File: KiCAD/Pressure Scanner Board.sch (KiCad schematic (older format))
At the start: 23 parts

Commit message: Pinned pressure sensors and added 3.3V - 5V level shifter
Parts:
- removed J? (x2): .1\" Headers, Pin_Headers:Pin_Header_Straight_1x20_Pitch2.54mm, symbol Conn_01x20
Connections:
- net labels removed: +5V, PA10, PA11, PA12, PA13, PA14, PA15, PA16, PA17, PA18, PA19, PA2, PA20, PA21, PA22, PA23, PA28, PA3, PA4, PA5, PA6, PA7, PA8, PA9, PB10, PB11, PB2, PB22, PB23, PB8, PB9, VIN
- wire segments 151 -> 78
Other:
- note removed: "0.100" Headers\n"

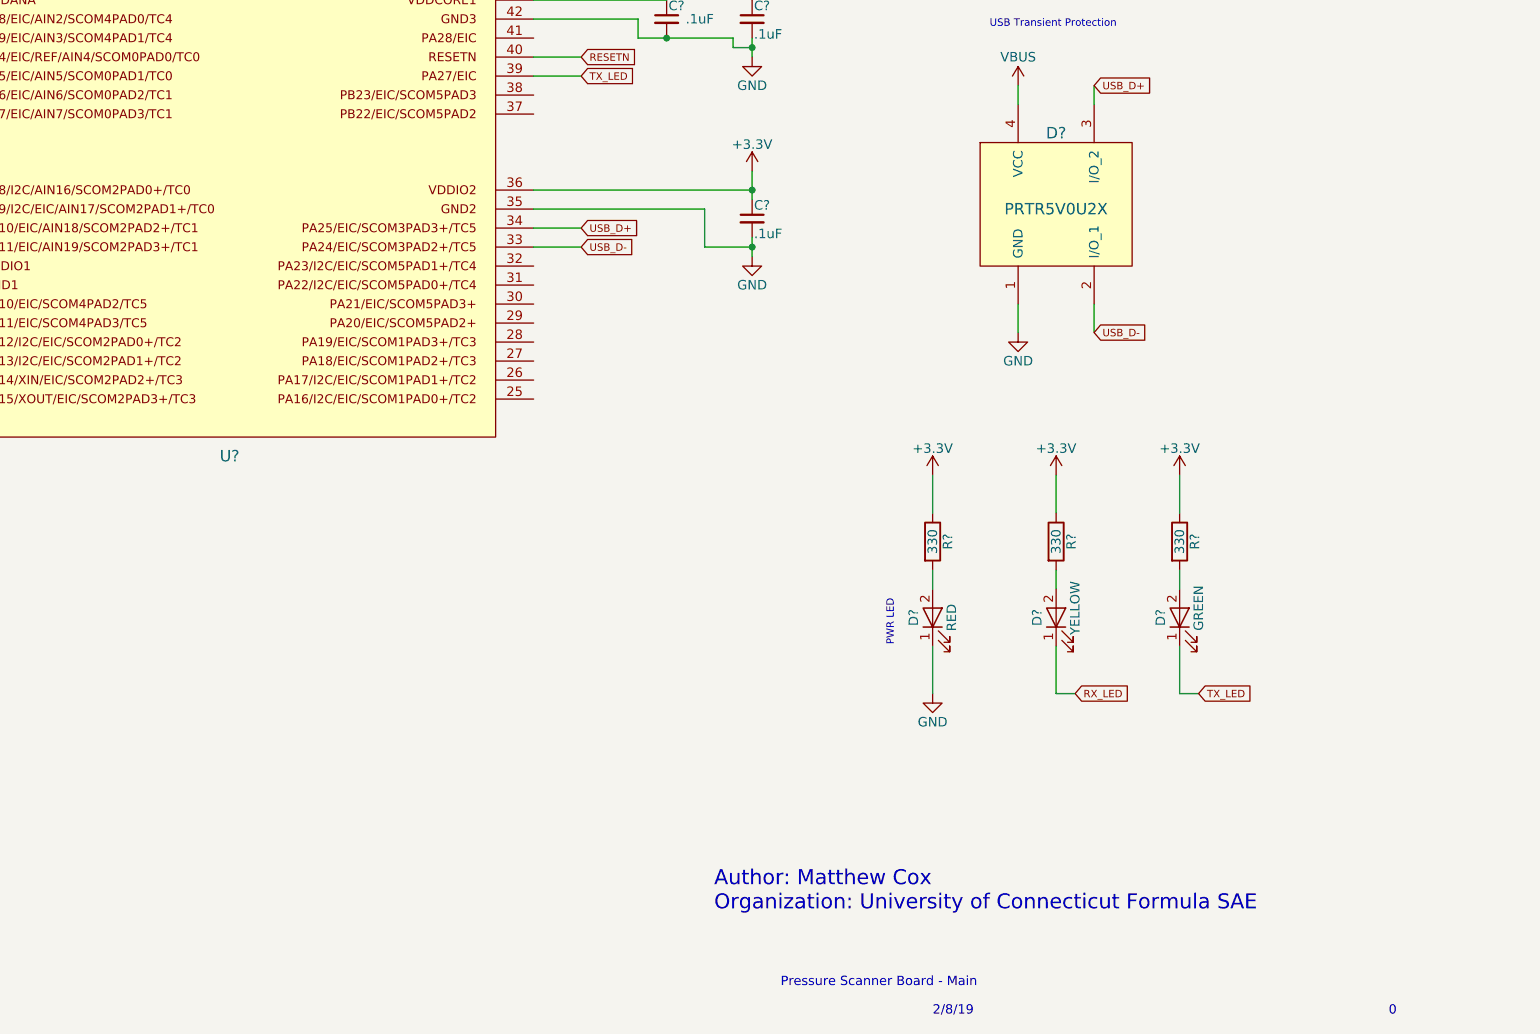
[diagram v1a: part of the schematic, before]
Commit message: Place power supply from SAMD21-Dev-Board
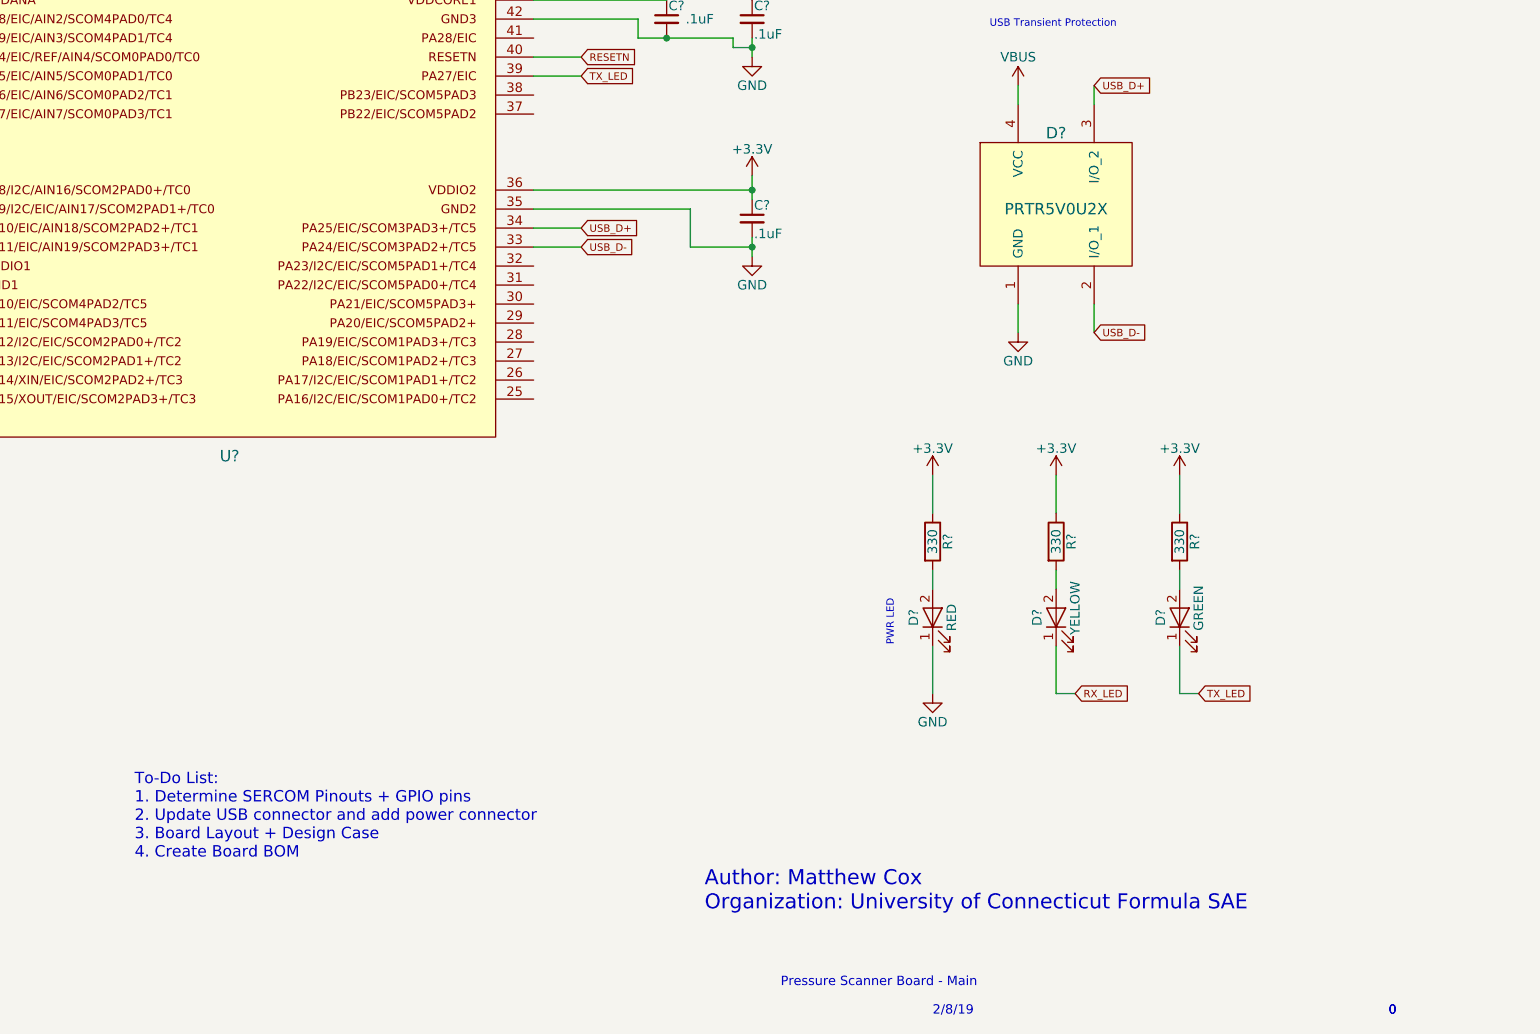
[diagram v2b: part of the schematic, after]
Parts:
- removed C?: .1uF, Capacitors_SMD:C_1206, symbol C_Small
- removed U?: SAMD21G18A-AU, symbol SAMD21G18A-AU
- added C?: .1uF, symbol C_Small
- added U?: SAMD21G18A-AU, symbol SAMD21G18A-AU
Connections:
- net +3V3: now also C?.1, U?.17, U?.36, U?.44
- net GND: now also C?.2, U?.18, U?.35, U?.42, U?.5
- net RESETN: now also U?.40
- net RX_LED: now also U?.48
- net SWCLK: now also U?.45
- net SWDIO: now also U?.46
- net TX_LED: now also U?.39
- net USB_D+: now also U?.34
- net USB_D-: now also U?.33
- net at C?.2, Y?.2: now also U?.2
- net at C?.2, Y?.1: now also U?.1
- net at C?.1: now also U?.43
- net at C?.1, C?.1, L?.2: now also U?.6
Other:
- note added: "0"
- note added: "To-Do List:\n1. Determine SERCOM Pinouts + GPIO pins\n2. Update USB connector and add power connector\n3. Board Layout + Design Case\n4. Create Board BOM"

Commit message: Added CAN Bus Sheet
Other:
- note added: "SWD Header"
- note added: "To-Do List:\n1. Determine SERCOM Pinouts + GPIO pins\n2. Update USB connector and add power connector\n3. Determine CAN Crystal Oscillator + Caps\n4. Board Layout + Design Case\n5. Create Board BOM"
- note removed: "SWD Debug Header"
- note removed: "To-Do List:\n1. Determine SERCOM Pinouts + GPIO pins\n2. Update USB connector and add power connector\n3. Board Layout + Design Case\n4. Create Board BOM"
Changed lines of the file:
@@
 LIBS:lm1117_edited
 LIBS:MF-MSMF050-2
+LIBS:mcp2515
+LIBS:mcp2551
+LIBS:cesd5v0ap
 LIBS:Pressure Scanner Board-cache
 EELAYER 25 0
@@
 $Descr A4 11693 8268
 encoding utf-8
-Sheet 1 3
+Sheet 1 4
 Title ""
 Date ""
@@
 Text GLabel 8950 5950 2    39   Input ~ 0
 RX_LED
-Text Notes 1800 5800 0    49   ~ 0
-SWD Debug Header
+Text Notes 1875 5800 0    49   ~ 0
+SWD Header
 $Comp
 L C_Small C?
@@
 Author: Matthew Cox\nOrganization: University of Connecticut Formula SAE
 Text Notes 4000 6825 0    60   ~ 0
-To-Do List:\n1. Determine SERCOM Pinouts + GPIO pins\n2. Update USB connector and add power connector\n3. Board Layout + Design Case\n4. Create Board BOM
+To-Do List:\n1. Determine SERCOM Pinouts + GPIO pins\n2. Update USB connector and add power connector\n3. Determine CAN Crystal Oscillator + Caps\n4. Board Layout + Design Case\n5. Create Board BOM
 $Comp
 L SAMD21G18A-AU U?
@@
 	6925 3400 6100 3400
 Connection ~ 7250 3600
+$Sheet
+S 10100 1750 500  175
+U 5C647E2E
+F0 "CAN Bus" 59
+F1 "CAN-BUS.sch" 59
+$EndSheet
 $EndSCHEMATC

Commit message: Schematic Rev 0
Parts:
- gave numbers to parts that had none: 21
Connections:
- net SS_3: now reaches U1.10
- net SS_4: now reaches U1.11
- net SS_5: now reaches U1.12
- net MISO_1: now reaches U1.13
- net SS_6: now reaches U1.14
- net MOSI_1: now reaches U1.15
- net SCLK_1: now reaches U1.16
- net MOSI_0: now reaches U1.19
- net SCLK_0: now reaches U1.20
- net MISO_0: now reaches U1.21
- net SS_7: now reaches U1.22
- net MISO_CAN: now reaches U1.25
- net SS_CAN: now reaches U1.26
- net MOSI_CAN: now reaches U1.27
- net SCLK_CAN: now reaches U1.28
- net SDA_L: now reaches U1.31
- net SCL_L: now reaches U1.32
- net SS_0: now reaches U1.7
- net SS_1: now reaches U1.8
- net SS_2: now reaches U1.9
- no-connect marks 4 -> 14
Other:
- note removed: "To-Do List:\n1. Determine SERCOM Pinouts + GPIO pins\n2. Update USB connector and add power connector\n3. Determine CAN Crystal Oscillator + Caps\n4. Board Layout + Design Case\n5. Create Board BOM"

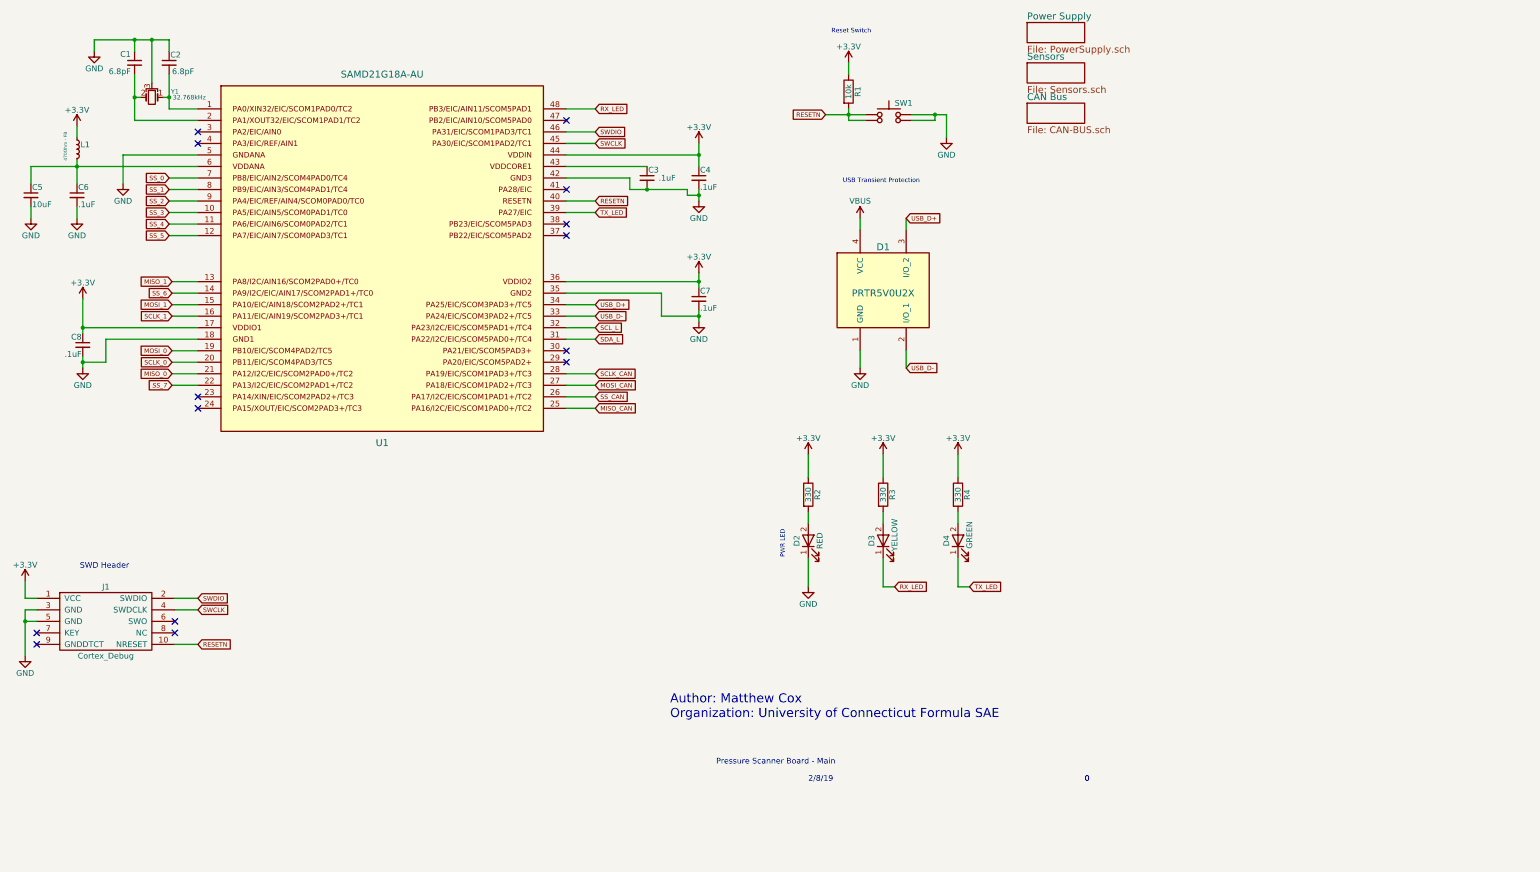
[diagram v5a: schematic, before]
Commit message: Added footprints for all components and created BOM
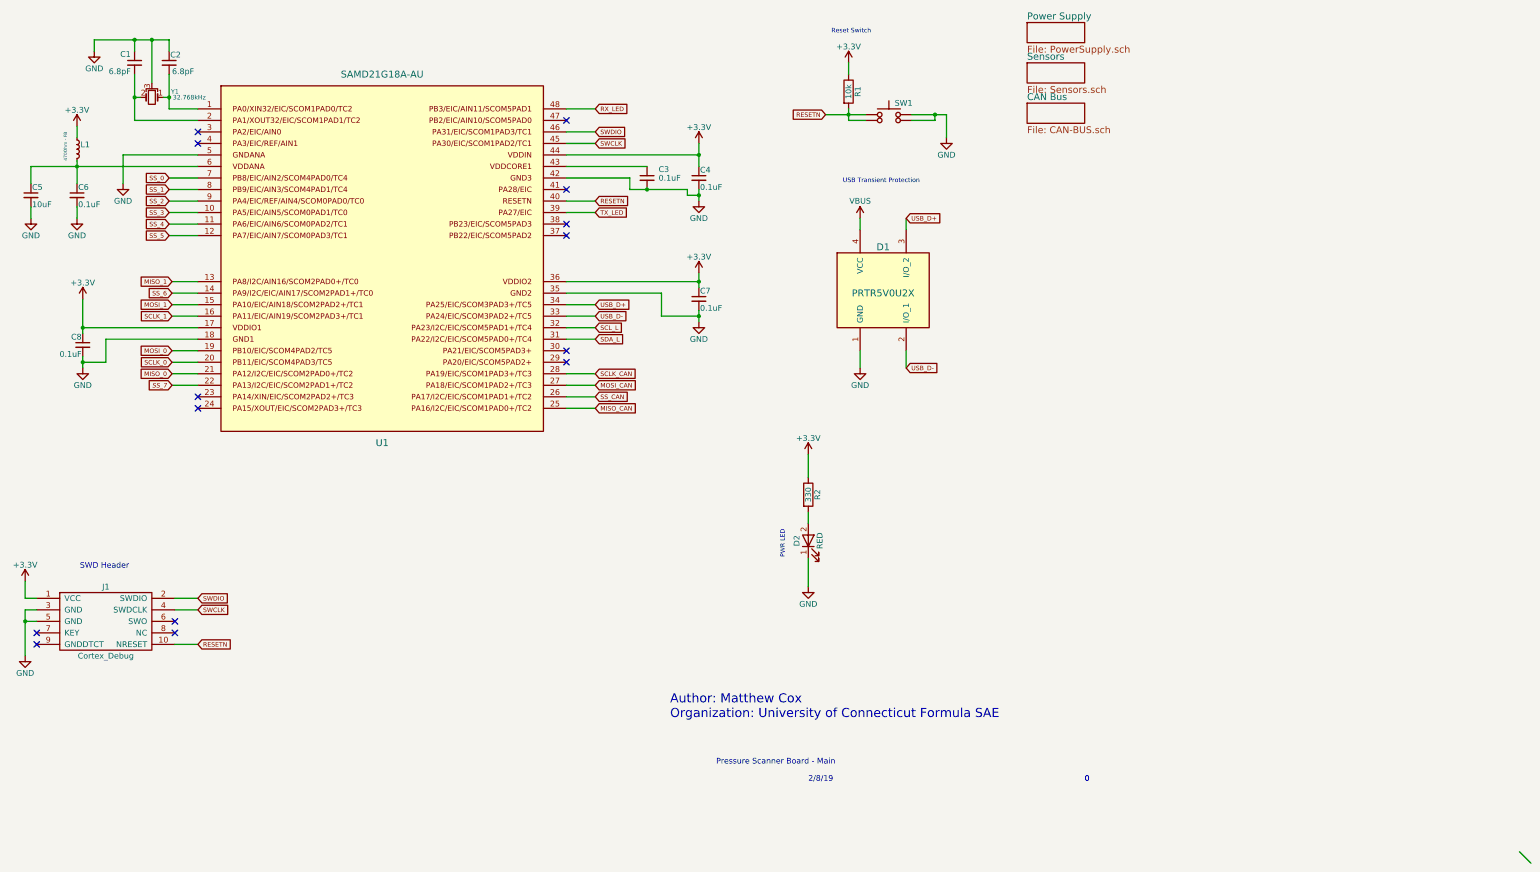
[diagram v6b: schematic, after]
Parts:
- removed D3: YELLOW, LEDs:LED_1206, symbol LED
- removed D4: GREEN, LEDs:LED_1206, symbol LED
- removed R3, R4: 330, Resistors_SMD:R_1210, symbol R
- C3, C4, C6, C8: value .1uF -> 0.1uF
- C7: value .1uF -> 0.1uF; footprint (none) -> Capacitors_SMD:C_1206
- SW1: value (none) -> FSMCTTR; footprint (none) -> FSMCTTR:FSMCTTR
- U1: footprint (none) -> ATSAMD21G18A-AU:QFP50P900X900X120-48N
- Y1: footprint MS1V-T1K:MS1V-T1K -> CMR200T:CMR200T
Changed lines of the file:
@@
 U 1 1 5C5DDD0A
 P 6800 2400
-F 0 "C3" H 6810 2470 50  0000 L CNN
-F 1 ".1uF" H 6900 2400 50  0000 L CNN
+F 0 "C3" H 6900 2475 50  0000 L CNN
+F 1 "0.1uF" H 6900 2400 50  0000 L CNN
 F 2 "Capacitors_SMD:C_1206" H 6800 2400 50  0001 C CNN
 F 3 "" H 6800 2400 50  0001 C CNN
@@
 P 1900 3850
 F 0 "C8" H 1910 3920 50  0000 L CNN
-F 1 ".1uF" H 1910 3770 50  0000 L CNN
+F 1 "0.1uF" H 1910 3770 50  0000 L CNN
 F 2 "Capacitors_SMD:C_1206" H 1900 3850 50  0001 C CNN
 F 3 "" H 1900 3850 50  0001 C CNN
@@
 P 7250 2400
 F 0 "C4" H 7260 2470 50  0000 L CNN
-F 1 ".1uF" H 7260 2320 50  0000 L CNN
+F 1 "0.1uF" H 7260 2320 50  0000 L CNN
 F 2 "Capacitors_SMD:C_1206" H 7250 2400 50  0001 C CNN
 F 3 "" H 7250 2400 50  0001 C CNN
@@
 P 1850 2550
 F 0 "C6" H 1860 2620 50  0000 L CNN
-F 1 ".1uF" H 1860 2470 50  0000 L CNN
+F 1 "0.1uF" H 1860 2470 50  0000 L CNN
 F 2 "Capacitors_SMD:C_1206" H 1850 2550 50  0001 C CNN
 F 3 "" H 1850 2550 50  0001 C CNN
@@
 	1    0    0    -1
 $EndComp
-Text GLabel 9600 5950 2    39   Input ~ 0
-TX_LED
-Text GLabel 8950 5950 2    39   Input ~ 0
-RX_LED
 Text Notes 1875 5800 0    49   ~ 0
 SWD Header
@@
 F 3 "" H 1450 2750 50  0001 C CNN
 	1    1450 2750
-	1    0    0    -1
-$EndComp
-$Comp
-L LED D3
-U 1 1 5C5DDD22
-P 8850 5550
-F 0 "D3" H 8850 5650 50  0000 C CNN
-F 1 "YELLOW" H 8900 5450 50  0000 C CNN
-F 2 "LEDs:LED_1206" H 8850 5550 50  0001 C CNN
-F 3 "" H 8850 5550 50  0001 C CNN
-	1    8850 5550
-	0    -1   -1   0
-$EndComp
-$Comp
-L LED D4
-U 1 1 5C5DDD23
-P 9500 5550
-F 0 "D4" H 9500 5650 50  0000 C CNN
-F 1 "GREEN" H 9550 5450 50  0000 C CNN
-F 2 "LEDs:LED_1206" H 9500 5550 50  0001 C CNN
-F 3 "" H 9500 5550 50  0001 C CNN
-	1    9500 5550
-	0    -1   -1   0
-$EndComp
-$Comp
-L R R3
-U 1 1 5C5DDD24
-P 8850 5150
-F 0 "R3" V 8930 5150 50  0000 C CNN
-F 1 "330" V 8850 5150 50  0000 C CNN
-F 2 "Resistors_SMD:R_1210" V 8780 5150 50  0001 C CNN
-F 3 "" H 8850 5150 50  0001 C CNN
-	1    8850 5150
-	1    0    0    -1
-$EndComp
-$Comp
-L R R4
-U 1 1 5C5DDD25
-P 9500 5150
-F 0 "R4" V 9580 5150 50  0000 C CNN
-F 1 "330" V 9500 5150 50  0000 C CNN
-F 2 "Resistors_SMD:R_1210" V 9430 5150 50  0001 C CNN
-F 3 "" H 9500 5150 50  0001 C CNN
-	1    9500 5150
 	1    0    0    -1
 $EndComp
@@
 $EndComp
 $Comp
-L +3.3V #PWR018
-U 1 1 5C5DDD2D
-P 8850 4800
-F 0 "#PWR018" H 8850 4650 50  0001 C CNN
-F 1 "+3.3V" H 8850 4940 50  0000 C CNN
-F 2 "" H 8850 4800 50  0001 C CNN
-F 3 "" H 8850 4800 50  0001 C CNN
-	1    8850 4800
-	1    0    0    -1
-$EndComp
-$Comp
-L +3.3V #PWR019
-U 1 1 5C5DDD2E
-P 9500 4800
-F 0 "#PWR019" H 9500 4650 50  0001 C CNN
-F 1 "+3.3V" H 9500 4940 50  0000 C CNN
-F 2 "" H 9500 4800 50  0001 C CNN
-F 3 "" H 9500 4800 50  0001 C CNN
-	1    9500 4800
-	1    0    0    -1
-$EndComp
-$Comp
 L Crystal_GND3_Small Y1
 U 1 1 5C5DDD30
@@
 F 0 "Y1" H 2300 1650 39  0000 C CNN
 F 1 "32.768kHz" H 2175 1700 39  0000 C CNN
-F 2 "MS1V-T1K:MS1V-T1K" H 2500 1700 50  0001 C CNN
+F 2 "CMR200T:CMR200T" H 2500 1700 50  0001 C CNN
 F 3 "" H 2500 1700 50  0001 C CNN
 	1    2500 1700
@@
 P 8900 1850
 F 0 "SW1" H 8950 1950 50  0000 L CNN
-F 1 " " H 8900 1700 50  0000 C CNN
-F 2 "" H 8900 2050 50  0001 C CNN
+F 1 " FSMCTTR" H 8900 1700 50  0001 C CNN
+F 2 "FSMCTTR:FSMCTTR" H 8900 2050 50  0001 C CNN
 F 3 "" H 8900 2050 50  0001 C CNN
 	1    8900 1850
@@
 F 0 "U1" H 4500 1500 60  0000 C CNN
 F 1 "SAMD21G18A-AU" H 4500 4700 60  0000 C CNN
-F 2 "" H 1400 2700 60  0001 C CNN
+F 2 "ATSAMD21G18A-AU:QFP50P900X900X120-48N" H 1400 2700 60  0001 C CNN
 F 3 "" H 1400 2700 60  0001 C CNN
 	1    4500 3100
@@
 P 7250 3450
 F 0 "C7" H 7260 3520 50  0000 L CNN
-F 1 ".1uF" H 7260 3370 50  0000 L CNN
-F 2 "" H 7250 3450 50  0001 C CNN
+F 1 "0.1uF" H 7260 3370 50  0000 L CNN
+F 2 "Capacitors_SMD:C_1206" H 7250 3450 50  0001 C CNN
 F 3 "" H 7250 3450 50  0001 C CNN
 	1    7250 3450
@@
 $EndComp
 $Comp
-L GND #PWR020
+L GND #PWR018
 U 1 1 5C632E4B
 P 7250 3650
-F 0 "#PWR020" H 7250 3400 50  0001 C CNN
+F 0 "#PWR018" H 7250 3400 50  0001 C CNN
 F 1 "GND" H 7250 3500 50  0000 C CNN
 F 2 "" H 7250 3650 50  0001 C CNN
@@
 $EndComp
 $Comp
-L +3.3V #PWR021
+L +3.3V #PWR019
 U 1 1 5C632E89
 P 7250 3225
-F 0 "#PWR021" H 7250 3075 50  0001 C CNN
+F 0 "#PWR019" H 7250 3075 50  0001 C CNN
 F 1 "+3.3V" H 7250 3365 50  0000 C CNN
 F 2 "" H 7250 3225 50  0001 C CNN
@@
 	1450 2450 1450 2300
 Wire Wire Line
-	8950 5950 8850 5950
-Wire Wire Line
-	8850 4800 8850 5000
-Wire Wire Line
-	9500 4800 9500 5000
-Wire Wire Line
-	8850 5400 8850 5300
-Wire Wire Line
-	8850 5950 8850 5700
-Wire Wire Line
-	9500 5700 9500 5950
-Wire Wire Line
-	9500 5950 9600 5950
-Wire Wire Line
-	9500 5400 9500 5300
-Wire Wire Line
 	8200 4800 8200 5000
 Wire Wire Line
@@
 NoConn ~ 6100 2500
 NoConn ~ 6100 1900
+Entry Wire Line
+	14375 8250 14475 8350
 $EndSCHEMATC

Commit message: Began routing, added differential pair labels
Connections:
- net OSC-: now reaches C1.2, U1.2, Y1.2
- net OSC+: now reaches C2.2, U1.1, Y1.1
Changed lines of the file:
@@
 Entry Wire Line
 	14375 8250 14475 8350
+Text Label 2650 1800 0    60   ~ 0
+OSC+
+Text Label 2650 1900 0    60   ~ 0
+OSC-
 $EndSCHEMATC

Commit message: Redoing layout
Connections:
- net RX_LED: no longer names the net of U1.48
- net TX_LED: no longer names the net of U1.39
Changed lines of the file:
@@
 Text GLabel 8350 1850 0    39   Input ~ 0
 RESETN
-Text GLabel 6350 1800 2    39   Input ~ 0
-RX_LED
 Text GLabel 6350 2000 2    39   Input ~ 0
 SWDIO
 Text GLabel 6350 2100 2    39   Input ~ 0
 SWCLK
-Text GLabel 6350 2700 2    39   Input ~ 0
-TX_LED
 $Comp
 L Cortex_Debug J1
@@
 	8350 1850 8700 1850
 Wire Wire Line
-	6100 1800 6350 1800
-Wire Wire Line
 	6100 2000 6350 2000
 Wire Wire Line
 	6100 2100 6350 2100
 Wire Wire Line
-	6100 2700 6350 2700
-Wire Wire Line
 	2700 6150 2900 6150
